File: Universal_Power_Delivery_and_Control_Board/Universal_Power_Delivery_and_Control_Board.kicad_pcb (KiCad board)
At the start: 4 copper layers, 99.5 x 69.3 mm, 181 parts, among them CN1 B03B-XASK-1-A(LF)(SN), CN2 B03B-XASK-1-A(LF)(SN), CN3 B03B-XASK-1-A(LF)(SN), CN4 B03B-XASK-1-A(LF)(SN), Q1 PMZ600UNEYL, Q2 PMZ600UNEYL, SW2 TS1102-TD35HBM, SW3 TS1102-TD35HBM, SW4 TS1102-TD35HBM, U1 TPS259470LRPWR, U10 SN74LVC1G17DCKR, U11 SN74LVC1G17DCKR, U12 SN74LVC1G17DCKR, U13 SN74LVC1G17DCKR, U14 SN74LVC1G17DCKR, U15 SN74LVC541APWR_C113281, U16 SN74LVC541APWR_C113281, U17 SN74LVC1G17DCKR, U18 LM66200DRLR, U19 TF-0803-0, U2 CH224Q_C46061833, U20 TCA9555PWR, U21 TPS22919DCK, U22 HC-PM254-8.5H-2X4PW-02A, U23 SN74LVC1G17DCKR, U3 USBLC6-2SC6, U4 ESD2CAN24-ES, U5 S2B-ZR (LF)(SN), U6 USBLC6-2SC6, U7 TPS54202DDC, U8 TPS51385RJNR, U9 TPS24751RUVR

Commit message: Finished layout 0 DRC errors.
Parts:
- removed U18: LM66200DRLR, lcsc_footprints:C3235556_SOT-583-8_L2_1-W1_2-P0_50-LS1_6-BL
- added C53: 100nF, Capacitor_SMD:C_0402_1005Metric_Pad0.74x0.62mm_HandSolder, F.Cu at (155.6, 91.4)
- added C54: 100nF, Capacitor_SMD:C_0402_1005Metric_Pad0.74x0.62mm_HandSolder, F.Cu at (161.2, 89.8)
- added C55: 2.2uF, Capacitor_SMD:C_0402_1005Metric_Pad0.74x0.62mm_HandSolder, F.Cu at (154.4, 91.4)
- added C56: 10uF, Capacitor_SMD:C_0805_2012Metric_Pad1.18x1.45mm_HandSolder, F.Cu at (110.5, 122.1)
- added C57: 1uF, Capacitor_SMD:C_0402_1005Metric_Pad0.74x0.62mm_HandSolder, F.Cu at (146.1, 89.6)
- added C58: 100nF, Capacitor_SMD:C_0402_1005Metric_Pad0.74x0.62mm_HandSolder, F.Cu at (148.8, 96.5)
- added CN5: XT30UPB-M, lcsc_footprints:C428721_CONN-TH_XT30UPB-M, F.Cu at (121.3, 112.5)
- added D6: SMD34PL-TP, lcsc_footprints:C725481_SOD-123FL_L2_8-W1_7-LS3_6-RD, F.Cu at (110.3, 84.0)
- added G***: LOGO, LOGO, F.Cu at (193.8, 134.5)
- added Q3: JTD2302, lcsc_footprints:C42443455_SOT-23-3_L2_9-W1_5-P2_0-LS2_5-BR, F.Cu at (189.8, 125.8)
- added R48: 1K, Resistor_SMD:R_0402_1005Metric_Pad0.72x0.64mm_HandSolder, F.Cu at (184.2, 95.6)
- added R49: 10K, Resistor_SMD:R_0402_1005Metric_Pad0.72x0.64mm_HandSolder, F.Cu at (187.2, 126.2)
- added R50: 1K02, Resistor_SMD:R_0402_1005Metric_Pad0.72x0.64mm_HandSolder, F.Cu at (150.8, 95.5)
- added R51: 10K, Resistor_SMD:R_0402_1005Metric_Pad0.72x0.64mm_HandSolder, F.Cu at (165.9, 81.6)
- added SW1: TSA016A2526A, lcsc_footprints:C2888428_SW-SMD_4P-L4_2-W3_3-P2_15-LS4_6, F.Cu at (159.7, 73.4)
- added TH1: 10K, Resistor_SMD:R_0402_1005Metric_Pad0.72x0.64mm_HandSolder, B.Cu at (117.7, 81.9)
- added U24: SC7A20HTR, lcsc_footprints:C19274408_LGA-12_L2_0-W2_0-P0_50-TL, F.Cu at (158.1, 90.0)
- added U25: S2B-ZR (LF)(SN), lcsc_footprints:C157930_CONN-TH_S2B-ZR-LF-SN, F.Cu at (188.7, 130.2)
- added U26: TPS2116DRL, Package_TO_SOT_SMD:SOT-583-8, F.Cu at (148.2, 92.9)
- C3: value 1uF -> 2.2uF
- D1: value SP1224-01UTG -> TVS2200DRVR; footprint lcsc_footprints:C3705881_DFN-2018-6A_L2_0-W1_8-P0_40-BL-EP -> lcsc_footprints:C523793_WSON-6_L2_0-W2_0-P0_65-BL-EP
- R23: value 1K -> 2K55
- moved H4 6.72 mm to (183.8, 130.2)
- moved R23 2.97 mm to (149.1, 94.8), turned to 0 degrees
- moved C20 0.43 mm to (111.5, 90.1)
- moved C21 0.43 mm to (111.5, 86.6)
- moved JP7 0.35 mm to (148.8, 90.2)
- moved JP8 0.35 mm to (148.8, 87.7)
- moved C3 0.29 mm to (110.8, 82.0)
- moved D1 0.18 mm to (118.0, 80.3), turned to 90 degrees
- moved R36 0.15 mm to (120.1, 81.6)
- moved R35 0.14 mm to (121.4, 81.6)
- moved C2 0.12 mm to (117.8, 81.8)
- moved C22 0.11 mm to (111.5, 92.0)
- moved C27 0.08 mm to (120.7, 99.5)
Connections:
- net /Digital_Signal_Output/CLK renamed /Power_Output/5V_O1
- net /Digital_Signal_Output/LE renamed /Power_Output/5V_O2
- net /Digital_Signal_Output/OE renamed /Power_Output/5V_O3
- net /PD_Section/CC1_read renamed /PD_Section/CC1_read_or_NTC
- A1 pad 30: unconnected-(A1-RUN-Pad30) -> Net-(A1-RUN)
- D1 pad 1: /PD_Section/PD_VBUS -> GND
- D1 pad 2: /PD_Section/PD_VBUS -> GND
- D1 pad 3: /PD_Section/PD_VBUS -> GND
- D1 pad 5: GND -> /PD_Section/PD_VBUS
- D1 pad 6: GND -> /PD_Section/PD_VBUS
- R23 pad 1: GND -> TPS54202_OUTPUT
- U20 pad 19: unconnected-(U20-P16-Pad19) -> Net-(U20-P16)
- U20 pad 20: unconnected-(U20-P17-Pad20) -> /BUZZ
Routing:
- net Net-(Q3-G): track 0.00 -> 39.7 mm, vias 0 -> 2
- net Net-(A1-RUN): track 0.00 -> 22.4 mm, vias 0 -> 1
- net /PD_Section/CC1_read_or_NTC: track 53.5 -> 74.7 mm
- net /BUZZ: track 0.00 -> 21.1 mm, vias 0 -> 2
- net Net-(U20-P16): track 0.00 -> 18.5 mm, vias 0 -> 2
- net +3V3: track 102.7 -> 91.7 mm, vias 60 -> 57
- net /SDA: track 89.1 -> 99.2 mm, vias 5 -> 7
- net /SCL: track 89.6 -> 95.3 mm
- net Net-(Q3-D): track 0.00 -> 4.66 mm
- net Net-(U20-P14): track 29.3 -> 24.6 mm
- net +5V_VSYS: track 7.94 -> 10.8 mm, vias 42 -> 57
- net GND: track 104.4 -> 107.1 mm, vias 550 -> 1176
- net TPS54202_OUTPUT: track 17.4 -> 19.1 mm
- net Net-(U26-PR1): track 1.09 -> 2.68 mm
- net /INT: track 18.0 -> 16.9 mm
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- added copper zone on In2.Cu, net GND
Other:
- board text added: "BUZ"
- board text added: "METUL"
- board text added: "RST"

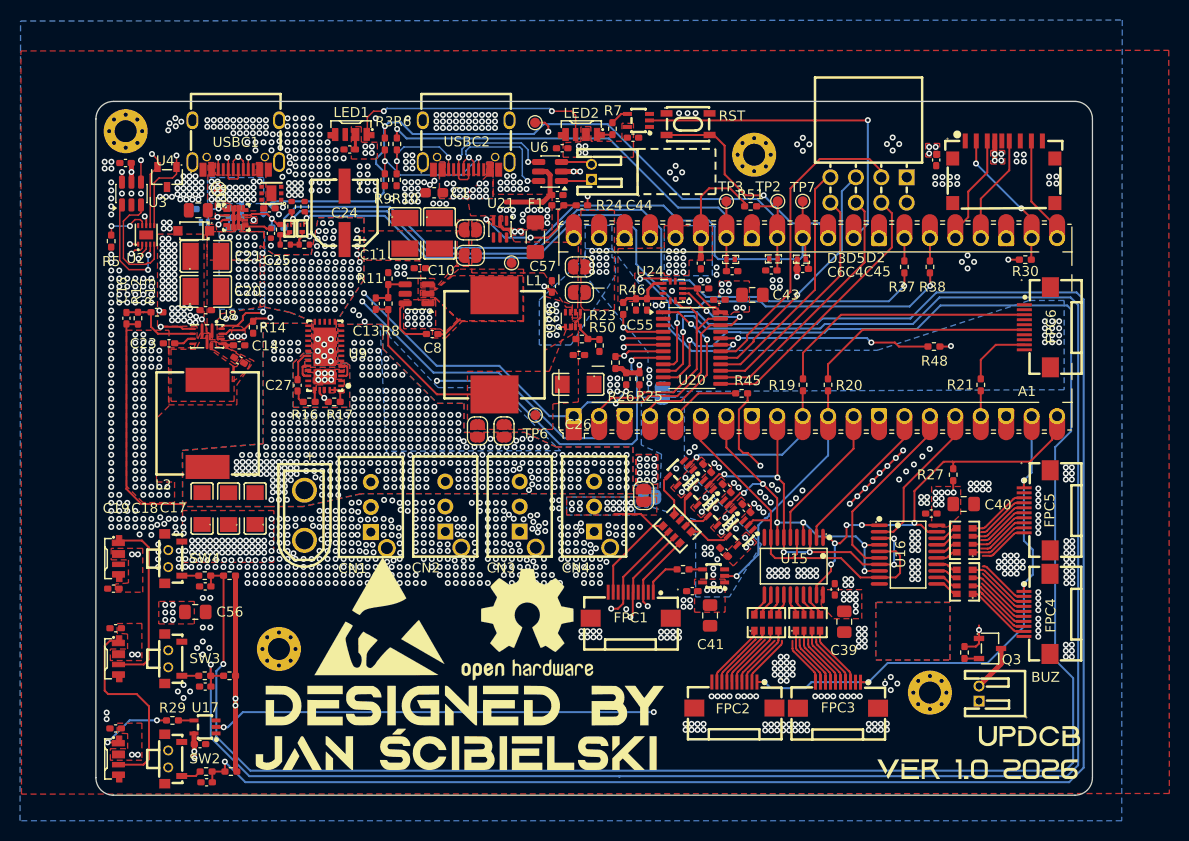
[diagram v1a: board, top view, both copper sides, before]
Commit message: Small mostly cosmetic changes and reannotation of the schematic, followed by the export of the gerber files for production.
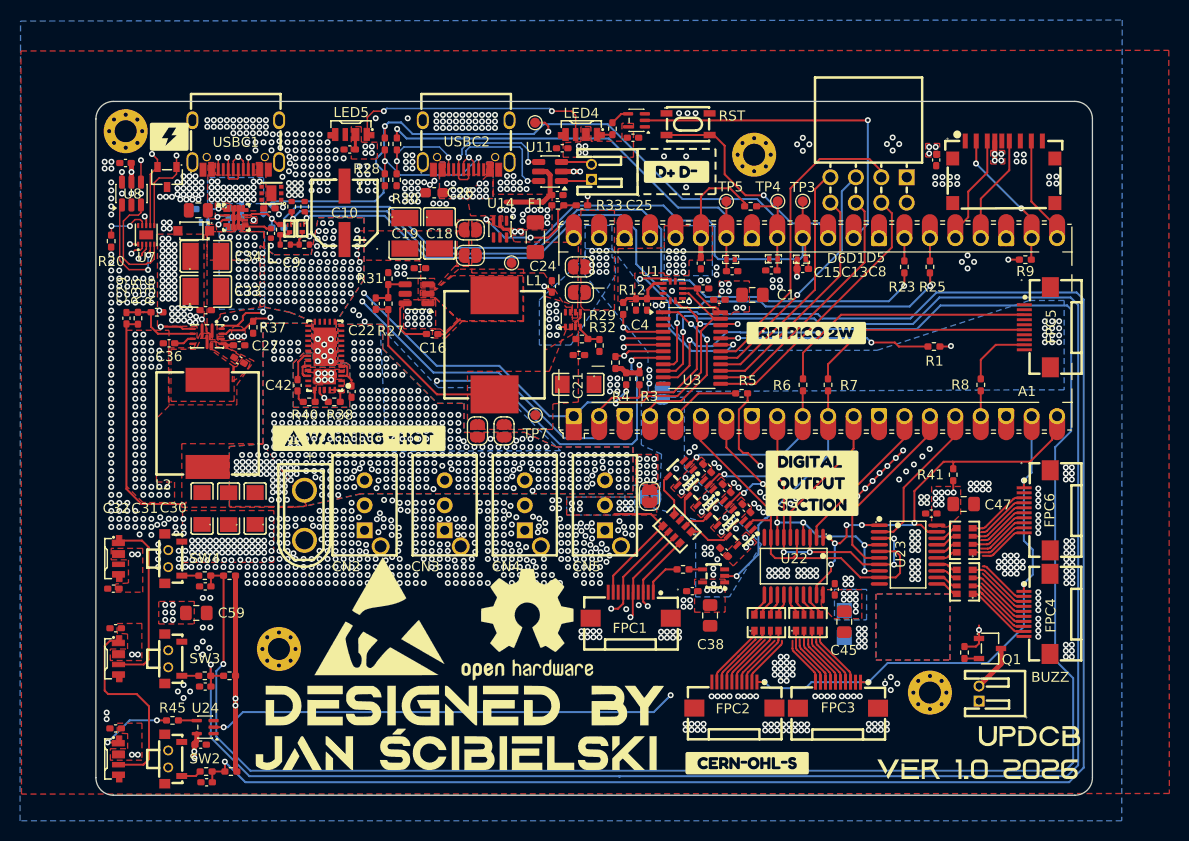
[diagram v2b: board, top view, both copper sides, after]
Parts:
- removed the C36 at (110.9, 135.3)
- removed the C56 at (110.5, 122.1)
- removed the U17 at (111.4, 133.6)
- removed the U23 at (154.7, 73.0)
- added C43: 100nF, Capacitor_SMD:C_0402_1005Metric_Pad0.74x0.62mm_HandSolder, F.Cu at (126.0, 100.1)
- added C49: 100nF, Capacitor_SMD:C_0402_1005Metric_Pad0.74x0.62mm_HandSolder, F.Cu at (111.0, 135.3)
- added C59: 10uF, Capacitor_SMD:C_0805_2012Metric_Pad1.18x1.45mm_HandSolder, F.Cu at (110.5, 122.2)
- added G***: LOGO, LOGO, F.Cu at (182.9, 119.1)
- added TP2: TestPoint, TestPoint:TestPoint_Pad_1.5x1.5mm, B.Cu at (175.2, 124.7)
- added U24: SN74LV1T34DCK, Package_TO_SOT_SMD:SOT-353_SC-70-5, F.Cu at (111.4, 133.6)
- added U25: SN74LV1T34DCK, Package_TO_SOT_SMD:SOT-353_SC-70-5, F.Cu at (154.5, 73.0)
- added kobee-studio-6AA92292: Kobee Studio, kobee-studio-6AA92292, B.Cu at (136.1, 127.8)
- added kobee-studio-6AA92370: Kobee Studio, kobee-studio-6AA92370, F.Cu at (165.6, 137.2)
- added kobee-studio-6AA926CC: Kobee Studio, kobee-studio-6AA92563, B.Cu at (187.2, 77.9)
- added kobee-studio-6AA92863: Kobee Studio, kobee-studio-6AA92822, F.Cu at (107.8, 74.7)
- added kobee-studio-6AA928EB: Kobee Studio, kobee-studio-6AA928EB, F.Cu at (126.8, 104.8)
- added kobee-studio-6AA9969D: Kobee Studio, kobee-studio-6AA9969D, F.Cu at (171.5, 94.2)
- added kobee-studio-6AA996C7: Kobee Studio, kobee-studio-6AA996C7, F.Cu at (172.0, 109.2)
- added kobee-studio-6AA99759: Kobee Studio, kobee-studio-6AA99759, F.Cu at (158.5, 78.2)
- C36: renamed from C23; value ? -> 100nF
- C4: renamed from C55; value 2.2uF -> 1uF
- C9: renamed from C25; value ? -> 4.7nF
- R10: renamed from R31; value ? -> 8K45
- R11: renamed from R32; value ? -> 16K2
- R13: renamed from R33; value ? -> 1K15
- R14: renamed from R34; value ? -> 11K3
- R17: renamed from R15; value ? -> 619R
- R19: renamed from R22; value ? -> 330R
- R21: renamed from R28; value ? -> 2370R
- R31: renamed from R11; value ? -> 15K
- R35: renamed from R12; value ? -> 120K
- TP1: value PD -> TestPoint; footprint TestPoint:TestPoint_Pad_D1.0mm -> TestPoint:TestPoint_Pad_1.5x1.5mm; moved to B.Cu
- moved TP1 75.4 mm to (175.2, 122.0)
- moved CN5 1.08 mm to (151.3, 111.5)
- moved CN2 0.65 mm to (127.3, 111.5)
- moved JP9 0.58 mm to (155.8, 110.5)
- moved CN4 0.52 mm to (143.3, 111.5)
- moved CN3 0.14 mm to (135.3, 111.5)
- renumbered C43 to C1, C24 to C10, C2 to C11, C3 to C12, C4 to C13, C12 to C14, C6 to C15, C8 to C16, C9 to C17, C10 to C18, C11 to C19, C42 to C2, C58 to C20, C26 to C21, C13 to C22, C46 to C23, C57 to C24, C44 to C25, C1 to C26, C14 to C27, C15 to C28, C16 to C29, C53 to C3, C17 to C30, C18 to C31, C19 to C32, C20 to C33, C21 to C34, C22 to C35, C28 to C37, C41 to C38, C29 to C39, C30 to C40, C31 to C41, C27 to C42, C32 to C44, C39 to C45, C33 to C46, C40 to C47, C34 to C48, C54 to C5, C35 to C50, C47 to C51, C48 to C52, C49 to C53, C50 to C54, C51 to C55, C52 to C56, C7 to C57, C5 to C58, C38 to C6, C37 to C7, C45 to C8, CN5 to CN1, CN1 to CN2, CN2 to CN3, CN3 to CN4, CN4 to CN5, D5 to D1, D1 to D2, D6 to D3, D2 to D5, D3 to D6, FPC6 to FPC5, FPC5 to FPC6, JP7 to JP1, JP8 to JP2, JP9 to JP3, JP10 to JP4, JP3 to JP5, JP11 to JP6, JP1 to JP7, JP2 to JP8, JP4 to JP9, LED3 to LED1, LED4 to LED2, LED5 to LED3, LED2 to LED4, LED1 to LED5, Q3 to Q1, Q1 to Q2, Q2 to Q3, R48 to R1, R46 to R12, R4 to R15, R51 to R16, R3 to R18, R49 to R2, R5 to R20, R6 to R22, R37 to R23, R36 to R24, R38 to R25, R35 to R26, R8 to R27, R9 to R28, R23 to R29, R25 to R3, R10 to R30, R50 to R32, R24 to R33, R47 to R34, R13 to R36, R14 to R37, R17 to R38, R18 to R39, R26 to R4, R16 to R40, R27 to R41, R39 to R42, R41 to R43, R43 to R44, R29 to R45, R40 to R46, R42 to R47, R44 to R48, R7 to R49, R45 to R5, R19 to R6, R20 to R7, R21 to R8, R30 to R9, TP7 to TP3, TP2 to TP4, TP3 to TP5, TP4 to TP6, TP6 to TP7, TP5 to TP8, U24 to U1, U5 to U10, U6 to U11, U7 to U12, U26 to U13, U21 to U14, U8 to U15, U10 to U16, U11 to U17, U12 to U18, U9 to U19, U25 to U2, U13 to U20, U14 to U21, U15 to U22, U16 to U23, U20 to U3, U22 to U4, U19 to U5, U1 to U6, U2 to U7, U3 to U8, U4 to U9
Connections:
- A1 pad 26: /PD_Section/MAX_current -> /PD_Section/H_current
- A1 pad 27: /PD_Section/H_current -> /PD_Section/MAX_current
- R23 pad 2: /PD_Section/H_current -> /PD_Section/MAX_current
- R25 pad 2: /PD_Section/MAX_current -> /PD_Section/H_current
- TP1 pad 1: /PD_Section/PD_VBUS -> +3V3
- U3 pad 22: /SDA -> /SCL
- U3 pad 23: /SCL -> /SDA
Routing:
- net /SDA: track 99.2 -> 95.5 mm, vias 7 -> 5
- net /SCL: track 95.3 -> 97.8 mm, vias 3 -> 5
- net +12V_PD: track 4.05 -> 5.30 mm
- net Net-(JP9-B): track 13.6 -> 14.0 mm, vias 14 -> 10
- net VOUT_connectors: vias 434 -> 441
- net GND: vias 1176 -> 1161
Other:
- board text added: "BUZZ"
- board text removed: "BUZ"
